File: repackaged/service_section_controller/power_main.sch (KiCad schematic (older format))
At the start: 17 parts

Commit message: changed labels and power nets and added fusing
changed relevant labels to global labels and checked that the
naming is correct. Changed vcc nets to corresponding 5v or 12v.
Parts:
- added F201, F202, F204, F205, F206: 500mA, footprints:Fuse_1210, symbol formula:F_500mA_16V
- gave numbers to parts that had none: 17
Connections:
- net labels added: +5V, +BATT, 12V_IMD, 12V_SHUTDOWN, 12V_TSAL, 5V_AIR_CONTROL, 5V_BMS
- net labels removed: +12V, VCC
- wire segments 39 -> 57
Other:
- note added: "Fusing Tree"
- note removed: "adding fusing tree\n"

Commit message: updated schematic
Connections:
- net +5V: no longer R205.1
- net at COUT201.1, COUT202.1, COUT203.1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: now also R205.1
- net 12v_BUCK: now reaches C201.1, C202.1, D201.1 (K), F203.2, R201.1, U201.4 (EN), U201.5 (VIN)
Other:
- note added: "12.8 - 16.8 V"
- note added: "FUSING TREE"
- note removed: "Fusing Tree"
- moved on the sheet: C201, C202, C203, COUT201, COUT202, COUT203, D201, D202, D203, F201, F202, F203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

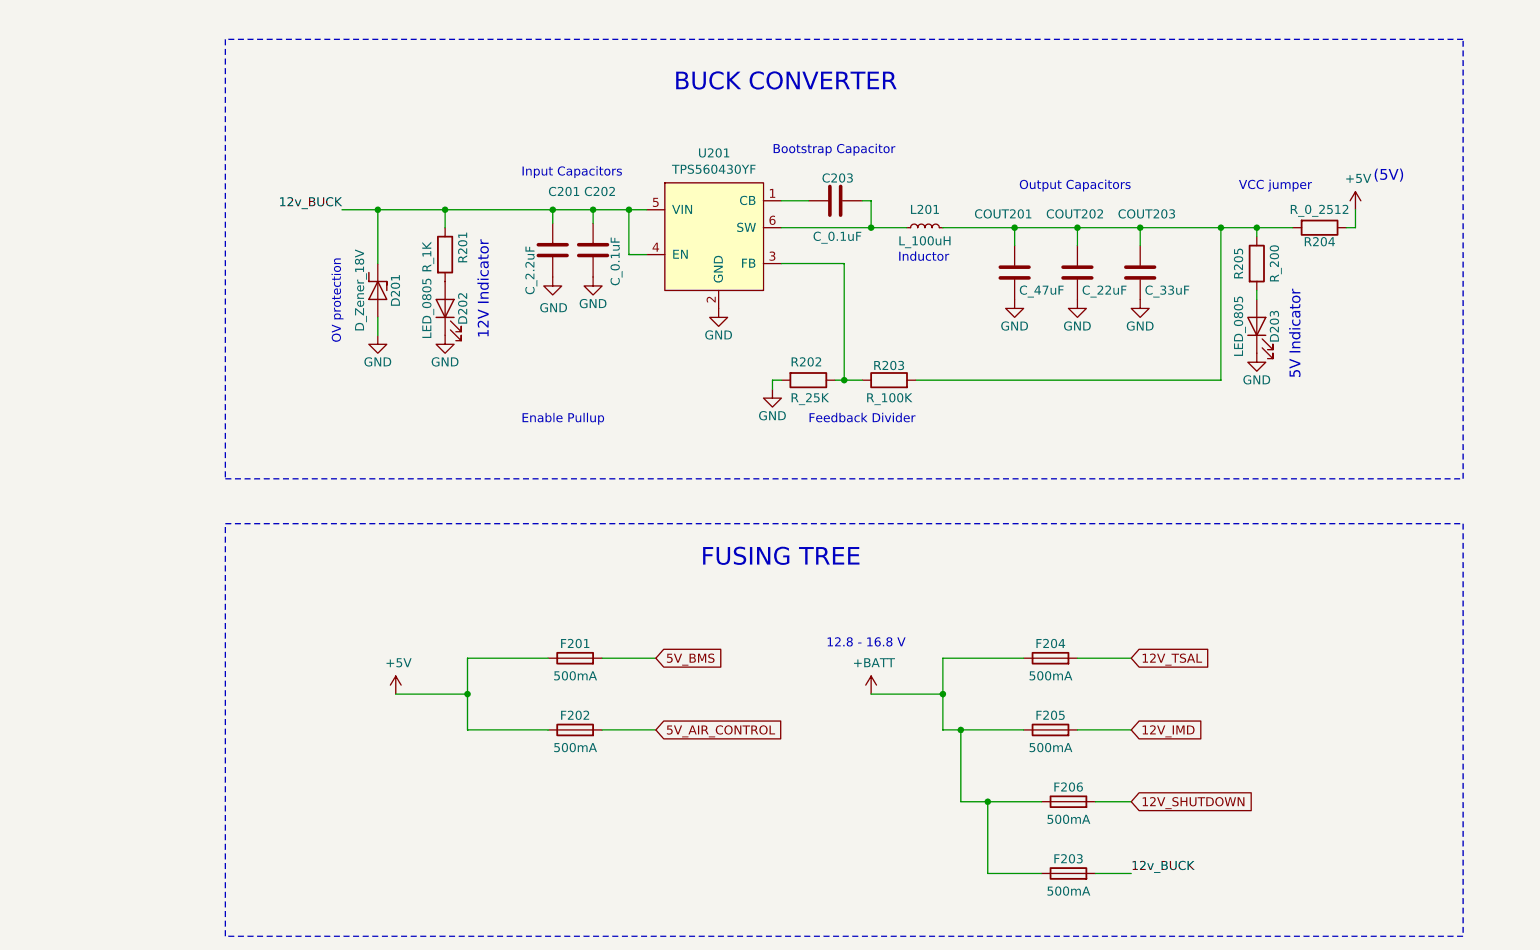
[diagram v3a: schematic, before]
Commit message: removed all traces and planes from layout. started adding test points
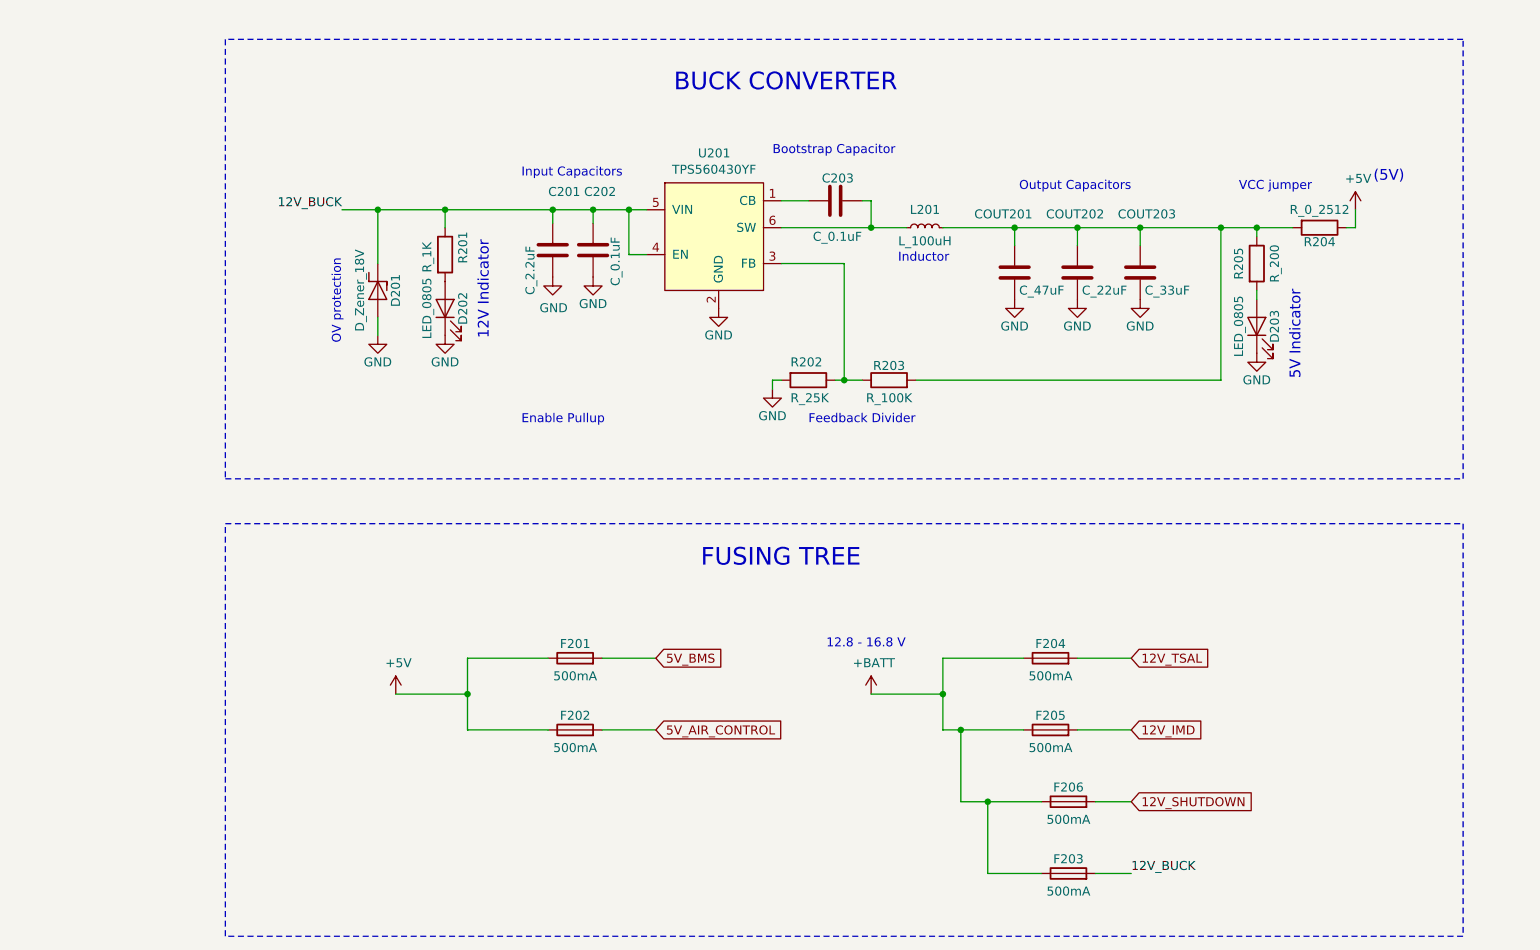
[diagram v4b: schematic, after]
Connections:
- net 12v_BUCK renamed 12V_BUCK
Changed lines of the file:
@@
 	6550 5200 6850 5200
 Text Label 7350 5600 0    50   ~ 0
-12v_BUCK
+12V_BUCK
 Wire Wire Line
 	7150 5600 7350 5600
 Text Label 2950 1900 2    50   ~ 0
-12v_BUCK
+12V_BUCK
 Wire Wire Line
 	7850 2000 8050 2000

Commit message: added test points and re-did schematic with new traces.
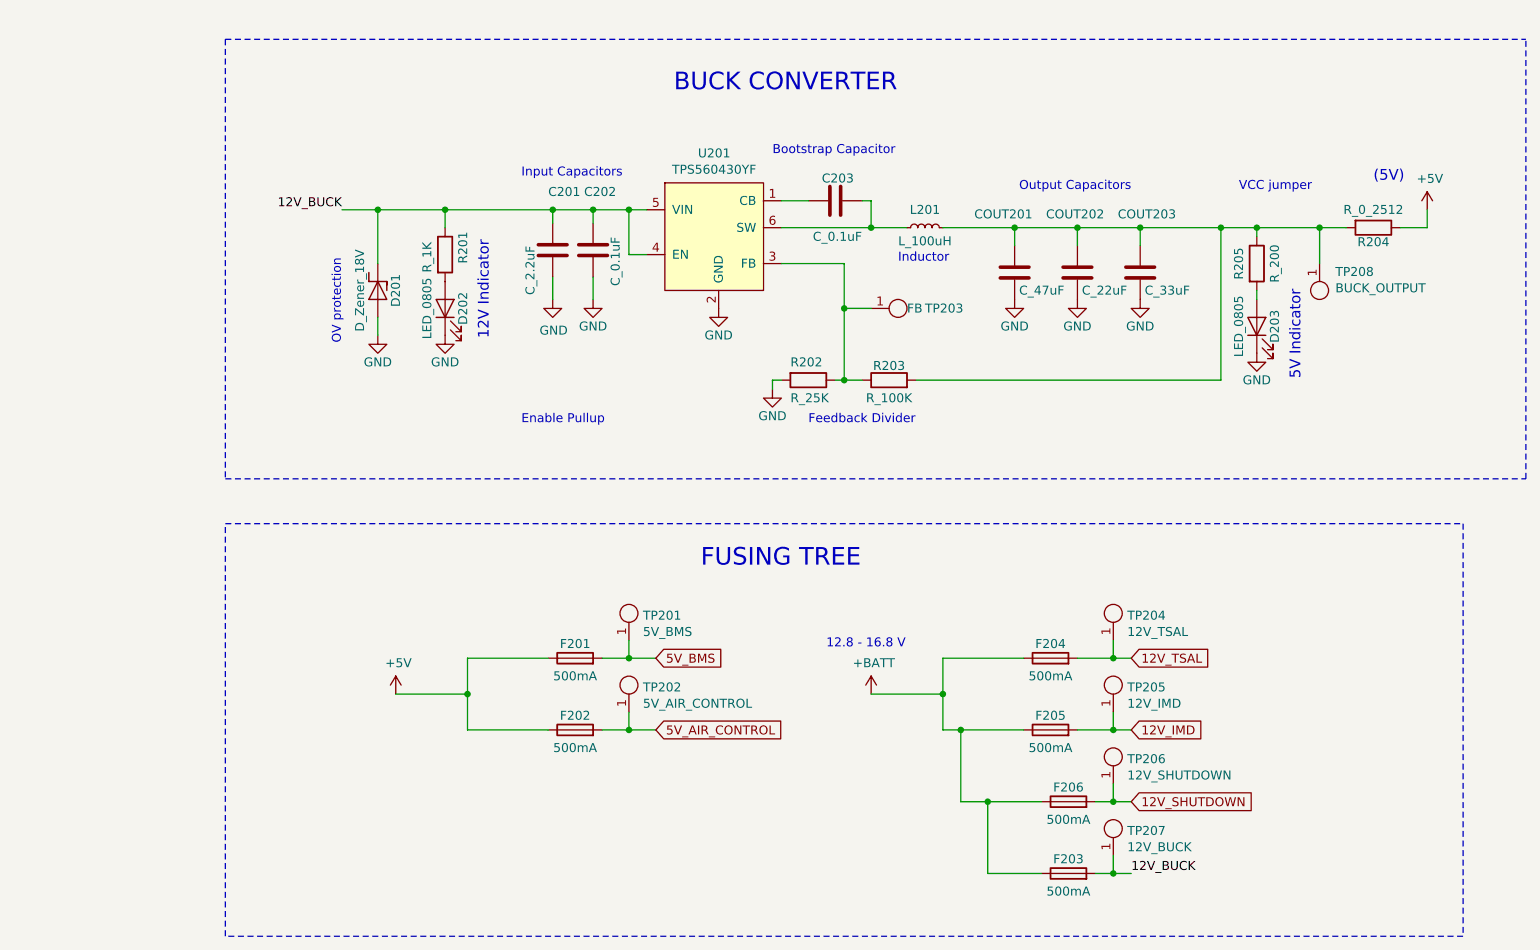
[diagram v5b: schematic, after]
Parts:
- added TP201: 5V_BMS, TestPoint:TestPoint_Pad_D1.0mm, symbol formula:Test_Point_SMD
- added TP202: 5V_AIR_CONTROL, TestPoint:TestPoint_Pad_D1.0mm, symbol formula:Test_Point_SMD
- added TP203: FB, TestPoint:TestPoint_Pad_D1.0mm, symbol formula:Test_Point_SMD
- added TP204: 12V_TSAL, TestPoint:TestPoint_Pad_D1.0mm, symbol formula:Test_Point_SMD
- added TP205: 12V_IMD, TestPoint:TestPoint_Pad_D1.0mm, symbol formula:Test_Point_SMD
- added TP206: 12V_SHUTDOWN, TestPoint:TestPoint_Pad_D1.0mm, symbol formula:Test_Point_SMD
- added TP207: 12V_BUCK, TestPoint:TestPoint_Pad_D1.0mm, symbol formula:Test_Point_SMD
- added TP208: BUCK_OUTPUT, TestPoint:TestPoint_Pad_D1.0mm, symbol formula:Test_Point_SMD
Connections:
- net 12V_BUCK: now also TP207.1
- net 12V_IMD: now also TP205.1
- net 12V_SHUTDOWN: now also TP206.1
- net 12V_TSAL: now also TP204.1
- net 5V_AIR_CONTROL: now also TP202.1
- net 5V_BMS: now also TP201.1
- net at COUT201.1, COUT202.1, COUT203.1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: now also TP208.1
- net at R202.1, R203.1, U201.3 (FB): now also TP203.1
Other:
- moved on the sheet: R204
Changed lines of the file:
@@
 L power:GND #PWR?
 U 1 1 60C4427E
-P 4350 2275
+P 4350 2400
 AR Path="/5C6B723E/60C4427E" Ref="#PWR?"  Part="1"
 AR Path="/60C4427E" Ref="#PWR?"  Part="1"
@@
 AR Path="/60A3B220/60C4427E" Ref="#PWR?"  Part="1"
 AR Path="/60A3B080/60C4427E" Ref="#PWR0103"  Part="1"
-F 0 "#PWR0103" H 4350 2025 50  0001 C CNN
-F 1 "GND" H 4350 2125 50  0000 C CNN
-F 2 "" H 4350 2275 50  0001 C CNN
-F 3 "" H 4350 2275 50  0001 C CNN
-	1    4350 2275
+F 0 "#PWR0103" H 4350 2150 50  0001 C CNN
+F 1 "GND" H 4350 2250 50  0000 C CNN
+F 2 "" H 4350 2400 50  0001 C CNN
+F 3 "" H 4350 2400 50  0001 C CNN
+	1    4350 2400
 	1    0    0    -1
 $EndComp
@@
 $EndComp
 Wire Wire Line
-	8600 2000 8600 1900
+	9000 2000 9000 1900
 $Comp
 L formula:R_10K R?
@@
 L formula:R_0_2512 R204
 U 1 1 60C442E2
-P 8400 2000
-F 0 "R204" V 8480 2000 50  0000 C CNN
-F 1 "R_0_2512" V 8300 2000 50  0000 C CNN
-F 2 "footprints:R_2512_OEM" H 8330 2000 50  0001 C CNN
-F 3 "http://www.te.com/commerce/DocumentDelivery/DDEController?Action=srchrtrv&DocNm=9-1773463-7&DocType=DS&DocLang=English" H 8480 2000 50  0001 C CNN
-F 4 "DK" H 8400 2000 60  0001 C CNN "MFN"
-F 5 "A121322CT-ND" H 8400 2000 60  0001 C CNN "MPN"
-F 6 "https://www.digikey.com/products/en?keywords=A121322CT-ND" H 8880 2400 60  0001 C CNN "PurchasingLink"
-	1    8400 2000
+P 8700 2000
+F 0 "R204" V 8780 2000 50  0000 C CNN
+F 1 "R_0_2512" V 8600 2000 50  0000 C CNN
+F 2 "footprints:R_2512_OEM" H 8630 2000 50  0001 C CNN
+F 3 "http://www.te.com/commerce/DocumentDelivery/DDEController?Action=srchrtrv&DocNm=9-1773463-7&DocType=DS&DocLang=English" H 8780 2000 50  0001 C CNN
+F 4 "DK" H 8700 2000 60  0001 C CNN "MFN"
+F 5 "A121322CT-ND" H 8700 2000 60  0001 C CNN "MPN"
+F 6 "https://www.digikey.com/products/en?keywords=A121322CT-ND" H 9180 2400 60  0001 C CNN "PurchasingLink"
+	1    8700 2000
 	0    1    1    0
 $EndComp
@@
 	6150 2850 7850 2850
 Wire Wire Line
-	5750 2850 5750 2200
+	5750 2850 5750 2450
 Connection ~ 5750 2850
 Wire Wire Line
@@
 L power:GND #PWR0112
 U 1 1 60C4435C
-P 4125 2275
-F 0 "#PWR0112" H 4125 2025 50  0001 C CNN
-F 1 "GND" H 4130 2102 50  0000 C CNN
-F 2 "" H 4125 2275 50  0001 C CNN
-F 3 "" H 4125 2275 50  0001 C CNN
-	1    4125 2275
+P 4125 2400
+F 0 "#PWR0112" H 4125 2150 50  0001 C CNN
+F 1 "GND" H 4130 2227 50  0000 C CNN
+F 2 "" H 4125 2400 50  0001 C CNN
+F 3 "" H 4125 2400 50  0001 C CNN
+	1    4125 2400
 	1    0    0    -1
 $EndComp
@@
 5V_AIR_CONTROL
 Wire Wire Line
-	4400 4400 4700 4400
-Wire Wire Line
-	4400 4800 4700 4800
+	4400 4400 4550 4400
+Wire Wire Line
+	4400 4800 4550 4800
 $Comp
 L formula:F_500mA_16V F?
@@
 	6300 4600 6300 4800
 Wire Wire Line
-	7050 4400 7350 4400
-Wire Wire Line
-	7050 4800 7350 4800
+	7050 4400 7250 4400
+Wire Wire Line
+	7050 4800 7250 4800
 Text GLabel 7350 4400 2    50   Input ~ 0
 12V_TSAL
@@
 L power:+5V #PWR0108
 U 1 1 60B59376
-P 8600 1900
-F 0 "#PWR0108" H 8600 1750 50  0001 C CNN
-F 1 "+5V" H 8615 2073 50  0000 C CNN
-F 2 "" H 8600 1900 50  0001 C CNN
-F 3 "" H 8600 1900 50  0001 C CNN
-	1    8600 1900
+P 9000 1900
+F 0 "#PWR0108" H 9000 1750 50  0001 C CNN
+F 1 "+5V" H 9015 2073 50  0000 C CNN
+F 2 "" H 9000 1900 50  0001 C CNN
+F 3 "" H 9000 1900 50  0001 C CNN
+	1    9000 1900
 	1    0    0    -1
 $EndComp
@@
 	6400 5200 6550 5200
 Wire Wire Line
-	7150 5200 7350 5200
+	7150 5200 7250 5200
 Text GLabel 7350 5200 2    50   Input ~ 0
 12V_SHUTDOWN
@@
 12V_BUCK
 Wire Wire Line
-	7150 5600 7350 5600
+	7150 5600 7250 5600
 Text Label 2950 1900 2    50   ~ 0
 12V_BUCK
@@
 Connection ~ 8050 2000
 Wire Wire Line
-	8550 2000 8600 2000
-Wire Wire Line
-	8050 2000 8250 2000
+	8850 2000 9000 2000
+Wire Wire Line
+	8050 2000 8400 2000
 Text Notes 5650 4350 0    50   ~ 0
 12.8 - 16.8 V
@@
 	2300 950  2300 3400
 Wire Notes Line
-	2300 3400 9200 3400
-Wire Notes Line
-	9200 3400 9200 950
-Wire Notes Line
-	9200 950  2300 950
+	9550 3400 9550 950
 Wire Notes Line
 	2300 3650 9200 3650
@@
 Wire Notes Line
 	2300 5950 2300 3650
+$Comp
+L formula:Test_Point_SMD TP201
+U 1 1 6142E745
+P 4550 4250
+F 0 "TP201" H 4628 4338 50  0000 L CNN
+F 1 "5V_BMS" H 4628 4247 50  0000 L CNN
+F 2 "TestPoint:TestPoint_Pad_D1.0mm" H 4550 4100 50  0001 C CNN
+F 3 "" H 4550 4250 50  0001 C CNN
+	1    4550 4250
+	1    0    0    -1
+$EndComp
+$Comp
+L formula:Test_Point_SMD TP202
+U 1 1 6142F46A
+P 4550 4650
+F 0 "TP202" H 4628 4738 50  0000 L CNN
+F 1 "5V_AIR_CONTROL" H 4628 4647 50  0000 L CNN
+F 2 "TestPoint:TestPoint_Pad_D1.0mm" H 4550 4500 50  0001 C CNN
+F 3 "" H 4550 4650 50  0001 C CNN
+	1    4550 4650
+	1    0    0    -1
+$EndComp
+Wire Wire Line
+	4550 4700 4550 4800
+Connection ~ 4550 4800
+Wire Wire Line
+	4550 4800 4700 4800
+Wire Wire Line
+	4550 4300 4550 4400
+Connection ~ 4550 4400
+Wire Wire Line
+	4550 4400 4700 4400
+$Comp
+L formula:Test_Point_SMD TP204
+U 1 1 61432017
+P 7250 4250
+F 0 "TP204" H 7328 4338 50  0000 L CNN
+F 1 "12V_TSAL" H 7328 4247 50  0000 L CNN
+F 2 "TestPoint:TestPoint_Pad_D1.0mm" H 7250 4100 50  0001 C CNN
+F 3 "" H 7250 4250 50  0001 C CNN
+	1    7250 4250
+	1    0    0    -1
+$EndComp
+$Comp
+L formula:Test_Point_SMD TP205
+U 1 1 6143273D
+P 7250 4650
+F 0 "TP205" H 7328 4738 50  0000 L CNN
+F 1 "12V_IMD" H 7328 4647 50  0000 L CNN
+F 2 "TestPoint:TestPoint_Pad_D1.0mm" H 7250 4500 50  0001 C CNN
+F 3 "" H 7250 4650 50  0001 C CNN
+	1    7250 4650
+	1    0    0    -1
+$EndComp
+$Comp
+L formula:Test_Point_SMD TP206
+U 1 1 61432D91
+P 7250 5050
+F 0 "TP206" H 7328 5138 50  0000 L CNN
+F 1 "12V_SHUTDOWN" H 7328 5047 50  0000 L CNN
+F 2 "TestPoint:TestPoint_Pad_D1.0mm" H 7250 4900 50  0001 C CNN
+F 3 "" H 7250 5050 50  0001 C CNN
+	1    7250 5050
+	1    0    0    -1
+$EndComp
+$Comp
+L formula:Test_Point_SMD TP207
+U 1 1 614355DE
+P 7250 5450
+F 0 "TP207" H 7328 5538 50  0000 L CNN
+F 1 "12V_BUCK" H 7328 5447 50  0000 L CNN
+F 2 "TestPoint:TestPoint_Pad_D1.0mm" H 7250 5300 50  0001 C CNN
+F 3 "" H 7250 5450 50  0001 C CNN
+	1    7250 5450
+	1    0    0    -1
+$EndComp
+Wire Wire Line
+	7250 4300 7250 4400
+Connection ~ 7250 4400
+Wire Wire Line
+	7250 4400 7350 4400
+Wire Wire Line
+	7250 4700 7250 4800
+Connection ~ 7250 4800
+Wire Wire Line
+	7250 4800 7350 4800
+Wire Wire Line
+	7250 5100 7250 5200
+Connection ~ 7250 5200
+Wire Wire Line
+	7250 5200 7350 5200
+Wire Wire Line
+	7250 5500 7250 5600
+Connection ~ 7250 5600
+Wire Wire Line
+	7250 5600 7350 5600
+$Comp
+L formula:Test_Point_SMD TP208
+U 1 1 614402AB
+P 8400 2250
+F 0 "TP208" H 8312 2246 50  0000 R CNN
+F 1 "BUCK_OUTPUT" H 8312 2337 50  0000 R CNN
+F 2 "TestPoint:TestPoint_Pad_D1.0mm" H 8400 2100 50  0001 C CNN
+F 3 "" H 8400 2250 50  0001 C CNN
+	1    8400 2250
+	-1   0    0    1
+$EndComp
+Wire Notes Line
+	2300 950  9550 950
+Wire Notes Line
+	2300 3400 9550 3400
+Wire Wire Line
+	8400 2000 8400 2200
+Connection ~ 8400 2000
+Wire Wire Line
+	8400 2000 8550 2000
+$Comp
+L formula:Test_Point_SMD TP203
+U 1 1 616409FB
+P 5950 2450
+F 0 "TP203" V 5950 2700 50  0000 L CNN
+F 1 "FB" V 5950 2600 50  0000 L CNN
+F 2 "TestPoint:TestPoint_Pad_D1.0mm" H 5950 2300 50  0001 C CNN
+F 3 "" H 5950 2450 50  0001 C CNN
+	1    5950 2450
+	0    1    1    0
+$EndComp
+Wire Wire Line
+	5750 2450 5900 2450
+Connection ~ 5750 2450
+Wire Wire Line
+	5750 2450 5750 2200
+Wire Wire Line
+	4125 2275 4125 2400
+Wire Wire Line
+	4350 2275 4350 2400
 $EndSCHEMATC
